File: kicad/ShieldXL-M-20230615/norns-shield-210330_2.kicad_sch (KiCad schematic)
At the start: 48 parts, among them J1 PJ-320B, J2 PJ-320B, SW1 PVA1, SW2 PVA1, SW3 PVA1, U5 HCPL-0631-500E

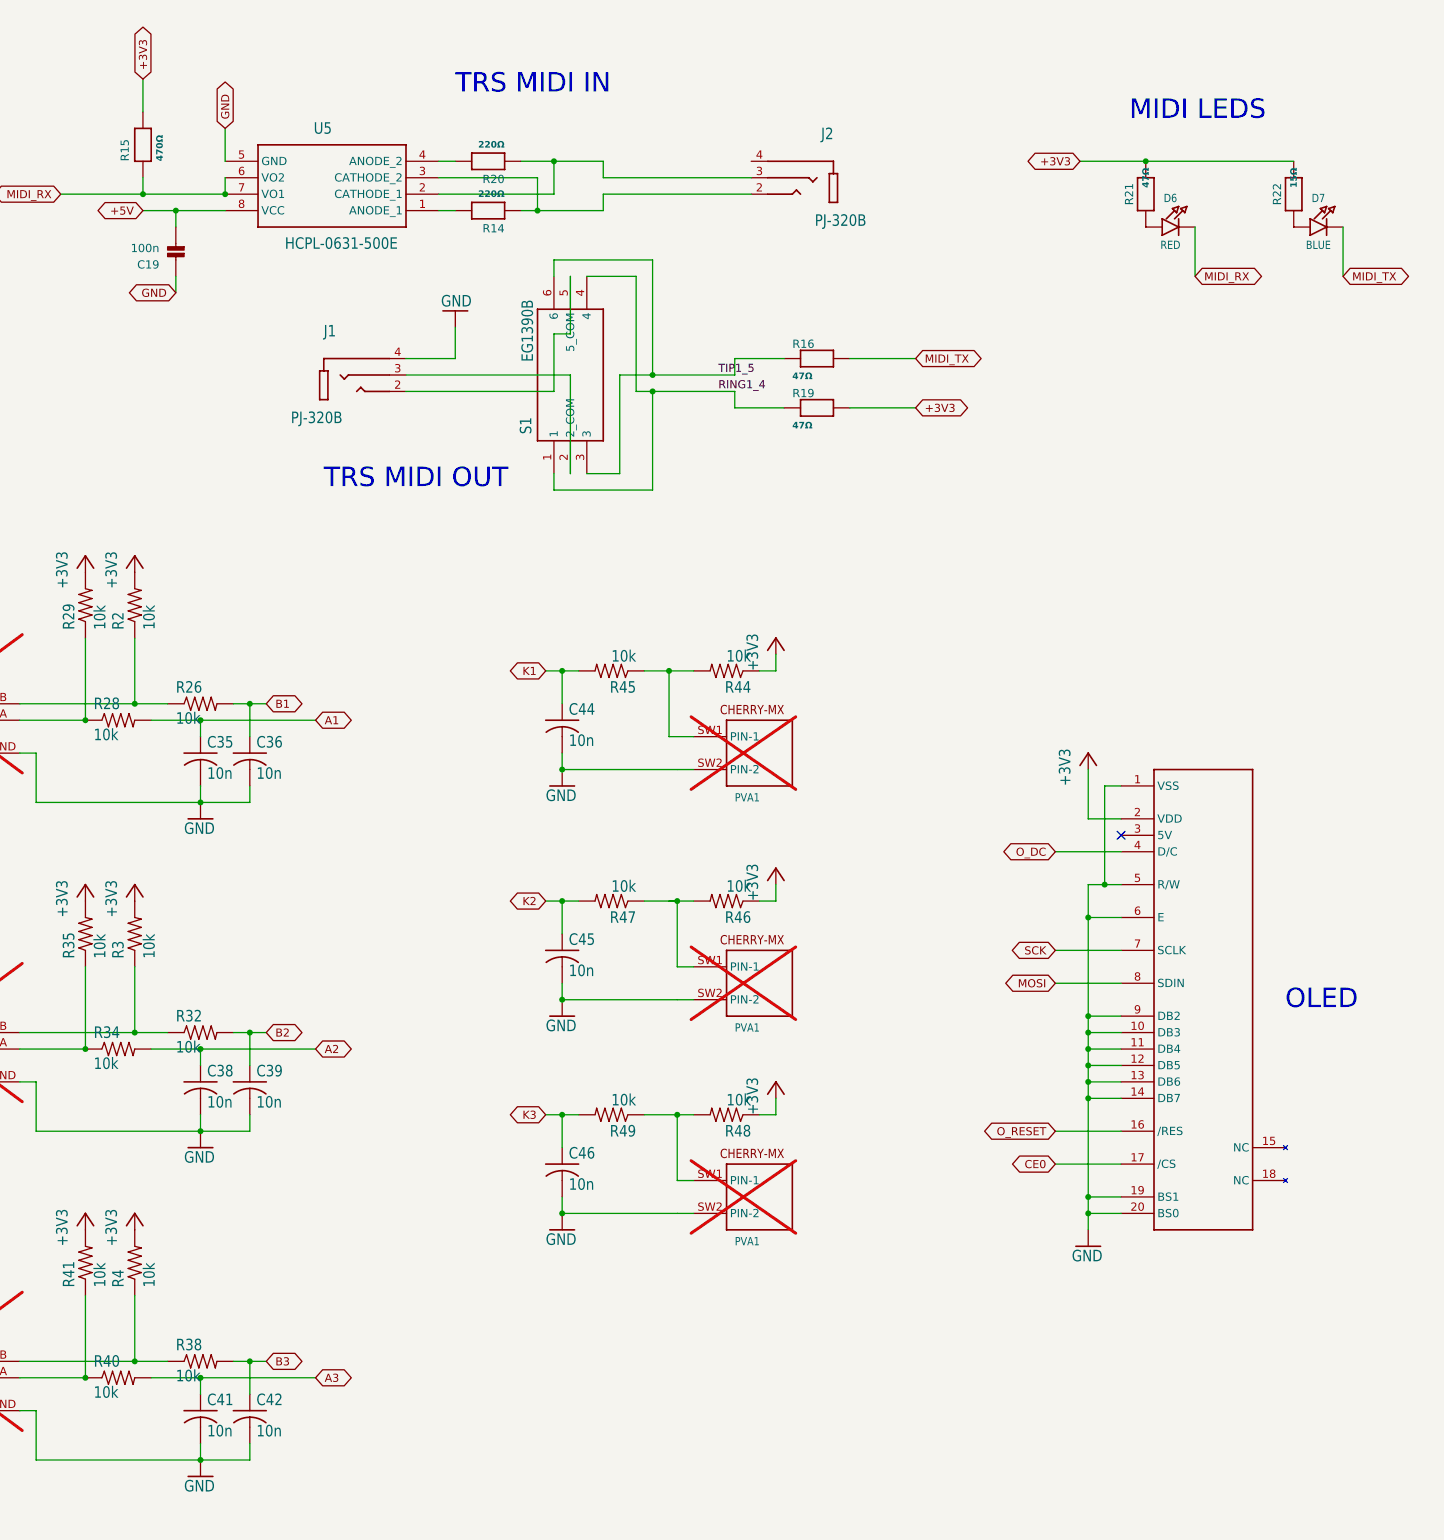
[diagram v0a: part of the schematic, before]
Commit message: updating JLCPCB codes
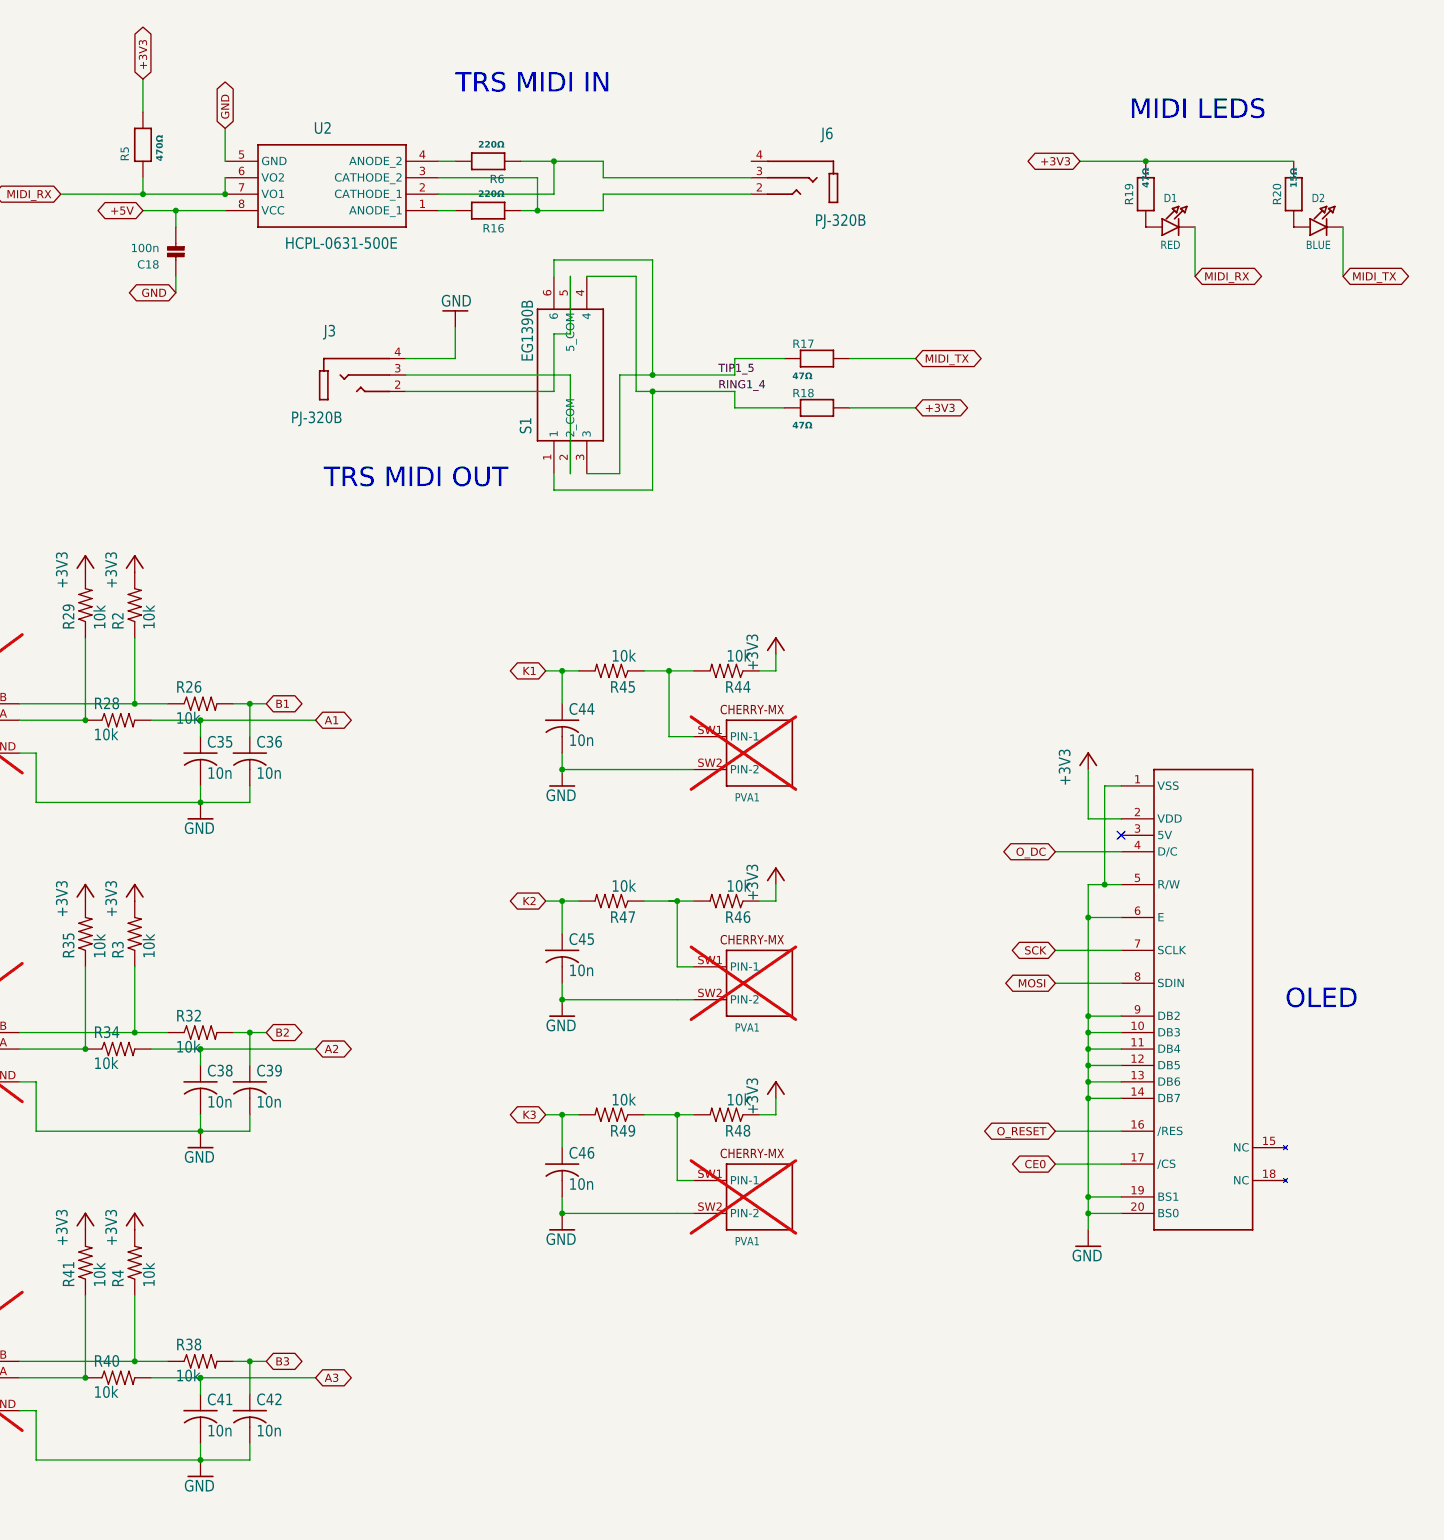
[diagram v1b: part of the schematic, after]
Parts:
- renumbered C19 to C18, D6 to D1, D7 to D2, J1 to J3, J2 to J6, R14 to R16, R16 to R17, R19 to R18, R21 to R19, R22 to R20, R15 to R5, R20 to R6, U5 to U2
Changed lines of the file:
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@@
 (kicad_sch
-	(version 20231120)
+	(version 20250114)
 	(generator "eeschema")
-	(generator_version "8.0")
+	(generator_version "9.0")
 	(paper "User" 443.23 305.206)
+	(text "TRS MIDI OUT"
+		(exclude_from_sim no)
+		(at 176.53 81.28 0)
+		(effects
+			(font
+				(size 3 3)
+			)
+			(justify left bottom)
+		)
+	)
+	(text "OLED"
+		(exclude_from_sim no)
+		(at 330.708 160.02 0)
+		(effects
+			(font
+				(size 3 3)
+			)
+		)
+	)
+	(text "MIDI LEDS"
+		(exclude_from_sim no)
+		(at 300.99 24.384 0)
+		(effects
+			(font
+				(size 3 3)
+			)
+			(justify left bottom)
+		)
+	)
+	(text "TRS MIDI IN"
+		(exclude_from_sim no)
+		(at 196.85 20.32 0)
+		(effects
+			(font
+				(size 3 3)
+			)
+			(justify left bottom)
+		)
+	)
 	(junction
 		(at 157.48 180.34)
@@
 		)
 	)
-	(text "TRS MIDI OUT"
-		(exclude_from_sim no)
-		(at 176.53 81.28 0)
-		(effects
-			(font
-				(size 3 3)
-			)
-			(justify left bottom)
-		)
-	)
-	(text "OLED"
-		(exclude_from_sim no)
-		(at 330.708 160.02 0)
-		(effects
-			(font
-				(size 3 3)
-			)
-		)
-	)
-	(text "MIDI LEDS"
-		(exclude_from_sim no)
-		(at 300.99 24.384 0)
-		(effects
-			(font
-				(size 3 3)
-			)
-			(justify left bottom)
-		)
-	)
-	(text "TRS MIDI IN"
-		(exclude_from_sim no)
-		(at 196.85 20.32 0)
-		(effects
-			(font
-				(size 3 3)
-			)
-			(justify left bottom)
-		)
-	)
 	(label "TIP1_5"
 		(at 237.49 63.5 0)
@@
 		(on_board yes)
 		(dnp no)
-		(property "Reference" "C19"
+		(property "Reference" "C18"
 			(at 151.13 45.72 0)
 			(effects
@@
 		(on_board yes)
 		(dnp no)
-		(property "Reference" "R21"
+		(property "Reference" "R19"
 			(at 300.99 35.56 0)
 			(effects
@@
 		(on_board yes)
 		(dnp no)
-		(property "Reference" "U5"
+		(property "Reference" "U2"
 			(at 177.8 25.4 0)
 			(effects
@@
 		(on_board yes)
 		(dnp no)
-		(property "Reference" "R19"
+		(property "Reference" "R18"
 			(at 248.92 67.0814 0)
 			(effects
@@
 		(on_board yes)
 		(dnp no)
-		(property "Reference" "D7"
+		(property "Reference" "D2"
 			(at 330.2 36.195 0)
 			(effects
@@
 		(on_board yes)
 		(dnp no)
-		(property "Reference" "D6"
+		(property "Reference" "D1"
 			(at 307.34 36.195 0)
 			(effects
@@
 		(on_board yes)
 		(dnp no)
-		(property "Reference" "R20"
+		(property "Reference" "R6"
 			(at 204.47 32.512 0)
 			(effects
@@
 		(on_board yes)
 		(dnp no)
-		(property "Reference" "R16"
+		(property "Reference" "R17"
 			(at 248.92 59.4614 0)
 			(effects
@@
 		(on_board yes)
 		(dnp no)
-		(property "Reference" "#GND3"
+		(property "Reference" "#GND06"
 			(at 196.85 53.594 0)
 			(effects
@@
 		(on_board yes)
 		(dnp no)
-		(property "Reference" "R15"
+		(property "Reference" "R5"
 			(at 146.558 30.48 0)
 			(effects
@@
 		(on_board yes)
 		(dnp no)
-		(property "Reference" "J1"
+		(property "Reference" "J3"
 			(at 176.5095 57.7621 0)
 			(effects
@@
 		(on_board yes)
 		(dnp no)
-		(property "Reference" "R14"
+		(property "Reference" "R16"
 			(at 204.47 40.132 0)
 			(effects
@@
 		(on_board yes)
 		(dnp no)
-		(property "Reference" "J2"
+		(property "Reference" "J6"
 			(at 255.2904 27.2821 0)
 			(effects
@@
 		(on_board yes)
 		(dnp no)
-		(property "Reference" "R22"
+		(property "Reference" "R20"
 			(at 323.85 35.56 0)
 			(effects
